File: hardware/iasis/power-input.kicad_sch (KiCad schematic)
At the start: 26 parts, among them J1001 USB4105-GF-A-120, Q1001 CSD18543Q3A, Q1002 CSD18543Q3A, U1001 LM74502DDFR, U1002 CH224Q, U1003 TPS26600PWPR

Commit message: Wire the schematic islands and side-match the RP2354 GPIOs
Each sheet now draws its circuits with wires. Labels remain at block edges
and on single-part islands: buttons, test points, decoupling and pull
resistors. The target-port page wires its hierarchical labels straight to
the child sheet pins, the ports page points its labels away from each
block, and the root sheet keeps every block clear of the title block.

The RP2354B GPIOs are reassigned so each signal leaves the package on the
side facing its destination. Update PCB from Schematic applied the 43
U1101 pad-net changes with no geometry change. Otherwise the netlist
matches the previous design, ERC keeps its 14 existing warnings and DRC
reports no parity issues.
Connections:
- no-connect marks 13 -> 11
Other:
- moved on the sheet: C1001, C1002, C1003, C1004, C1005, C1006, D1001, J1001, Q1001, Q1002, R1001, R1002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

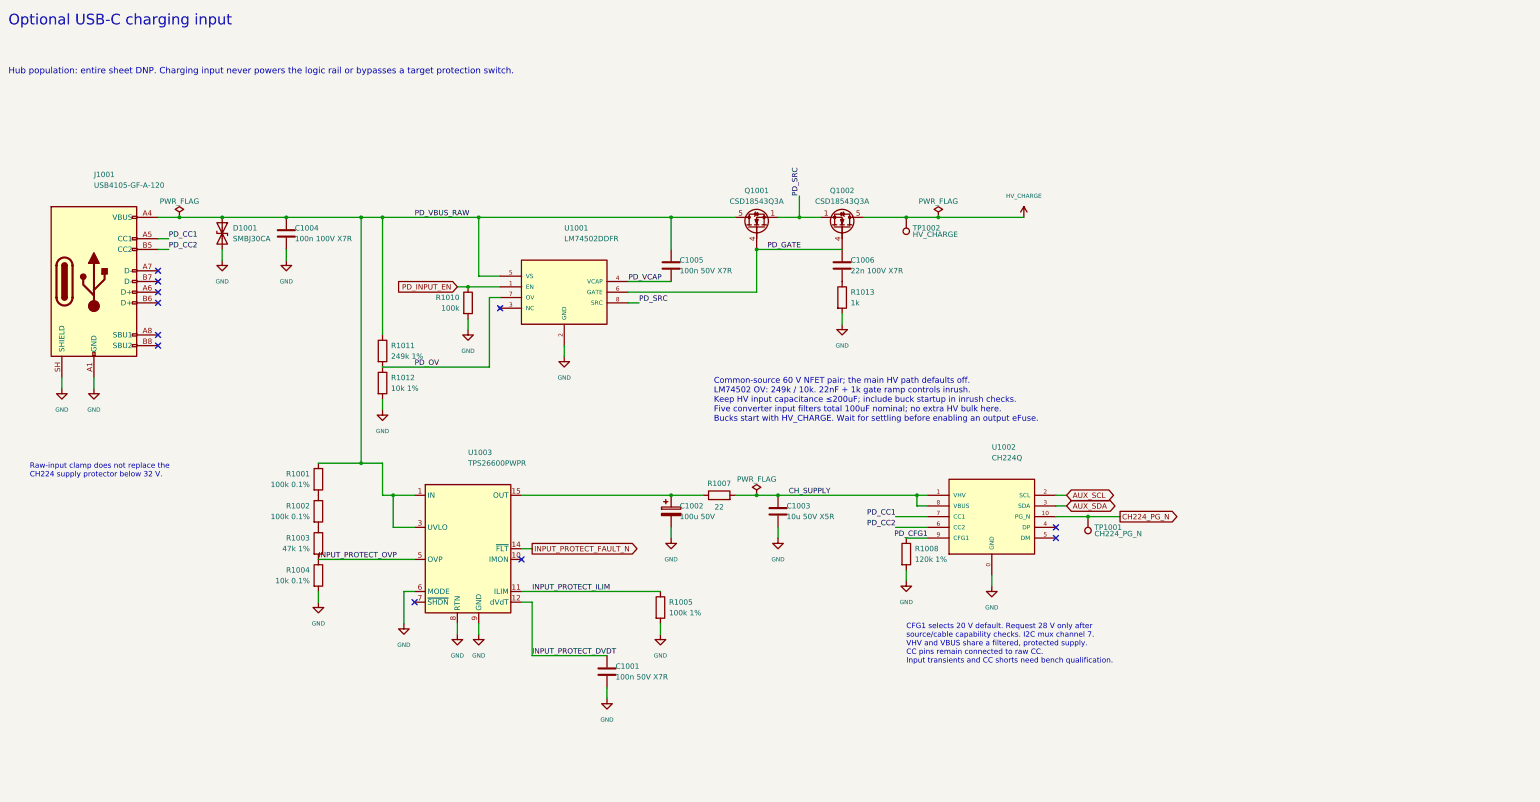
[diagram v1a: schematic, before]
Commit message: Redraw the power input, host power and logic supply sheets
The charging input, host power budget and logic supply sheets follow
the power path left to right: connector and protection, switches and
eFuses, then the converters with their feedback and output capacitors.
Supply rails use power symbols with their existing net names, notes sit
beside their circuits, and each sheet carries a title, date and
revision. The netlist is unchanged.
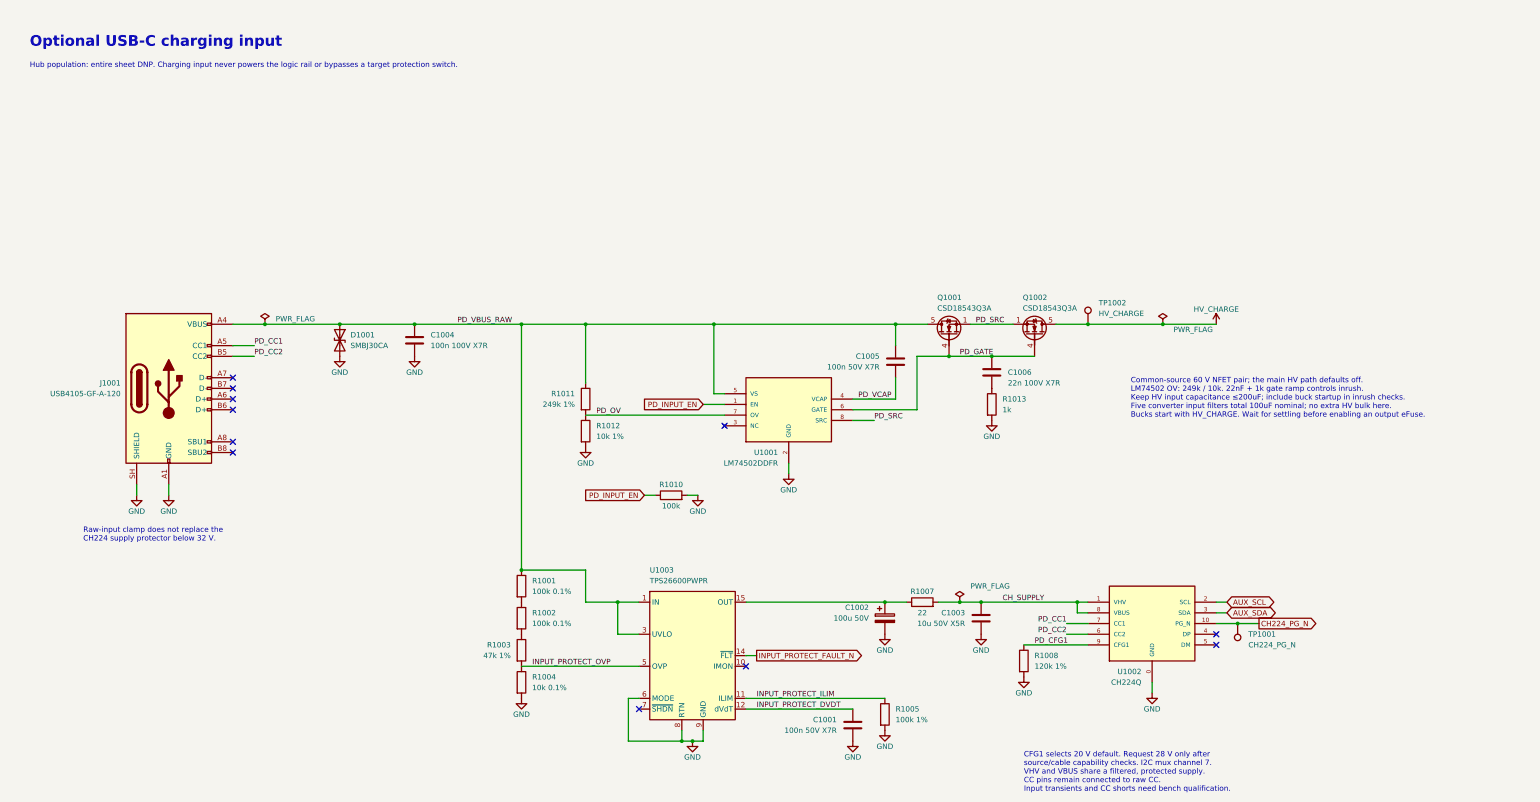
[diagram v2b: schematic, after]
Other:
- title: (none) -> Optional USB-C charging input
- moved on the sheet: C1001, C1002, C1003, C1004, C1005, C1006, D1001, J1001, Q1001, Q1002, R1001, R1002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

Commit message: Drill every via and thermal via at 0.3 mm
JLC prices 0.2 and 0.25 mm holes as a small-via tier that also forces
TG155 and a 4-wire Kelvin test: $39.18 on a five-board order. With
every plated hole at 0.3 mm or more the board quotes in the standard
tier.

- 2,005 vias keep their pads (0.45, 0.55, 0.6 mm) and drill 0.3 mm.
- U201's VQFN-100, the WQFN-20 and the HTSSOP-16 ThermalVias
  footprints move to Iasis.pretty copies with 0.3 mm thermal vias
  (121 holes); the schematic links follow.
- Rules match JLC's published via limits: 0.2 mm via hole to copper
  and hole to hole, 0.075 mm annular ring, 0.3 mm minimum hole.

DRC with refill and parity: 0 errors, 0 warnings, 0 unconnected.
Pour island counts unchanged; ERC unchanged at 14.
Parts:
- U1003: footprint Package_SO:HTSSOP-16-1EP_4.4x5mm_P0.65mm_EP3.4x5mm_Mask2.66x2.46mm_ThermalVias -> Iasis:HTSSOP-16-1EP_4.4x5mm_P0.65mm_EP3.4x5mm_Mask2.66x2.46mm_ThermalVias
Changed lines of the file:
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@@
 			)
 		)
-		(property "Footprint" "Package_SO:HTSSOP-16-1EP_4.4x5mm_P0.65mm_EP3.4x5mm_Mask2.66x2.46mm_ThermalVias"
+		(property "Footprint" "Iasis:HTSSOP-16-1EP_4.4x5mm_P0.65mm_EP3.4x5mm_Mask2.66x2.46mm_ThermalVias"
 			(at 182.88 147.32 0)
 			(hide yes)

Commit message: Use smaller charge inductors and bulk capacitors, and solder pads for debug
The 6.8 uH PSTMAA666460 (12.5 A saturation) replaces the 10 uH 11 x 10 mm
inductor, a 6.3 mm 35 V hybrid capacitor the 10 mm 50 V bulk capacitor on
each charging buck, and an 8 mm 68 uF part the 100 uF on the charging input.
SWD and UART become three solder pads each in Raspberry Pi debug order.
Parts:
- C1002: value 100u 50V -> 68u 50V; footprint Capacitor_SMD:CP_Elec_10x10.5 -> Capacitor_SMD:CP_Elec_8x10.5; LCSC C109086 -> C178645; MPN EEHZA1H101P -> EEHZC1H680P
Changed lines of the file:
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@@
 			)
 		)
-		(property "Value" "100u 50V"
+		(property "Value" "68u 50V"
 			(at 224.79 158.75 0)
 			(show_name no)
@@
 			)
 		)
-		(property "Footprint" "Capacitor_SMD:CP_Elec_10x10.5"
+		(property "Footprint" "Capacitor_SMD:CP_Elec_8x10.5"
 			(at 231.14 158.75 0)
 			(hide yes)
@@
 			)
 		)
-		(property "Datasheet" "https://www.lcsc.com/datasheet/lcsc_datasheet_2304140030_PANASONIC-EEHZA1H101P_C109086.pdf"
+		(property "Datasheet" "https://datasheet.lcsc.com/datasheet/pdf/d3106b7be65c7347fb943a2e324d3be8.pdf"
 			(at 231.14 158.75 0)
 			(hide yes)
@@
 			)
 		)
-		(property "Description" "Unpolarized capacitor"
+		(property "Description" "Polarized capacitor"
 			(at 231.14 158.75 0)
 			(hide yes)
@@
 			)
 		)
-		(property "LCSC" "C109086"
+		(property "LCSC" "C178645"
 			(at 231.14 158.75 0)
 			(hide yes)
@@
 			)
 		)
-		(property "MPN" "EEHZA1H101P"
+		(property "MPN" "EEHZC1H680P"
 			(at 231.14 158.75 0)
 			(hide yes)
